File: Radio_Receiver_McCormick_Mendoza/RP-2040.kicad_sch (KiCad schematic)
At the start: 0 parts

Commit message: Merge conflict resolution.
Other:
- title: (none) -> Radio Receiver
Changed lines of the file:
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@@
 	(paper "A4")
 	(title_block
+		(title "Radio Receiver")
 		(date "2026-04-19")
 		(rev "0.0.1")

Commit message: Propogated Title Block Fields
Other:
- company: (none) -> Walla Walla University
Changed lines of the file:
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@@
 		(date "2026-04-19")
 		(rev "0.0.1")
+		(company "Walla Walla University")
 		(comment 2 "Daniel Mendoza")
 		(comment 3 "Jeffrey McCormick")

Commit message: Added switchable antenna filters and photos.
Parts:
- added J21: Conn_01x20_Socket, Connector_PinSocket_2.54mm:PinSocket_1x20_P2.54mm_Vertical, symbol Connector:Conn_01x20_Socket
- added J22: Conn_01x01_Pin, Connector_PinHeader_2.54mm:PinHeader_1x01_P2.54mm_Vertical, symbol Connector:Conn_01x01_Pin
- added J23: Conn_01x20_Socket, Intro_to_CAD:PinSocket_1x20_P2.54mm_Vertical-pins21-40, symbol Connector:Conn_01x20_Socket
- added JP50: USB Only, Jumper:SolderJumper-2_P1.3mm_Open_RoundedPad1.0x1.5mm, symbol Jumper:Jumper_2_Open
- added R29: 20kΩ, PCM_JLCPCB:R_0805, symbol PCM_JLCPCB-Resistors:0805,20kΩ
- added S1: Tactile Button, 160gf, PCM_JLCPCB:SW_TS-1088-AR02016, symbol PCM_JLCPCB-Connectors_Buttons:Tactile Button, 160gf, 12V, 50mA, 4.0mm
- added U13: Pico, MCU_RaspberryPi_and_Boards:RPi_Pico_SMD_TH, symbol MCU_RaspberryPi_and_Boards:Pico
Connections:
- new net: J21.1 (Pin_1), U13.1 (GPIO0)
- new net: J21.10 (Pin_10), U13.10 (GPIO7)
- new net: J21.11 (Pin_11), U13.11 (GPIO8)
- new net: J21.12 (Pin_12), U13.12 (GPIO9)
- new net: J21.14 (Pin_14), U13.14 (GPIO10)
- new net: J21.15 (Pin_15), U13.15 (GPIO11)
- new net: J21.16 (Pin_16), U13.16 (GPIO12)
- new net: J21.17 (Pin_17), U13.17 (GPIO13)
- new net: J21.19 (Pin_19), U13.19 (GPIO14)
- new net: J21.2 (Pin_2), U13.2 (GPIO1)
- new net: J21.20 (Pin_20), U13.20 (GPIO15)
- new net: J23.21 (Pin_20), U13.21 (GPIO16)
- new net: J23.22 (Pin_19), U13.22 (GPIO17)
- new net: J23.24 (Pin_17), U13.24 (GPIO18)
- new net: J23.25 (Pin_16), U13.25 (GPIO19)
- new net: J23.26 (Pin_15), U13.26 (GPIO20)
- new net: J23.27 (Pin_14), U13.27 (GPIO21)
- new net: J23.29 (Pin_12), U13.29 (GPIO22)
- new net: J23.31 (Pin_10), U13.31 (GPIO26_ADC0)
- new net: J23.32 (Pin_9), U13.32 (GPIO27_ADC1)
- new net: J23.33 (Pin_8), U13.33 (AGND)
- new net: J23.34 (Pin_7), U13.34 (GPIO28_ADC2)
- new net: J23.35 (Pin_6), U13.35 (ADC_VREF)
- new net: J23.36 (Pin_5), U13.36 (3V3)
- new net: J23.37 (Pin_4), U13.37 (3V3_EN)
- new net: J23.39 (Pin_2), U13.39 (VSYS)
- new net: J21.4 (Pin_4), U13.4 (GPIO2)
- new net: J22.1 (Pin_1), J23.40 (Pin_1), JP50.1 (A), U13.40 (VBUS)
- new net: J21.5 (Pin_5), U13.5 (GPIO3)
- new net: J21.6 (Pin_6), U13.6 (GPIO4)
- new net: J21.7 (Pin_7), U13.7 (GPIO5)
- new net: J21.9 (Pin_9), U13.9 (GPIO6)
- new net +3.3V: R29.1
- new net GND: J21.13 (Pin_13), J21.18 (Pin_18), J21.3 (Pin_3), J21.8 (Pin_8), J23.23 (Pin_18), J23.28 (Pin_13), J23.38 (Pin_3), S1.2 (B), U13.13 (GND), U13.18 (GND), U13.23 (GND), U13.28 (GND), U13.3 (GND), U13.38 (GND), U13.8 (GND)
- new net RST: J23.30 (Pin_11), R29.2, S1.1 (A), U13.30 (RUN)
- new net VDDA: JP50.2 (B)
- no-connect marks 0 -> 3
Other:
- note added: "If you are using a real Pico, his jumper bridges a Schottky diode from USB in to Vsys (4.7v with it open, 5.0v from USB port with it soldered)"
- note added: "These jumpers are for changing GPIO pins if necessary. They also allow you to connect modules similar to a breadboard."
- note added: "V+ (YD-RP2040) VBUS (Pico)"

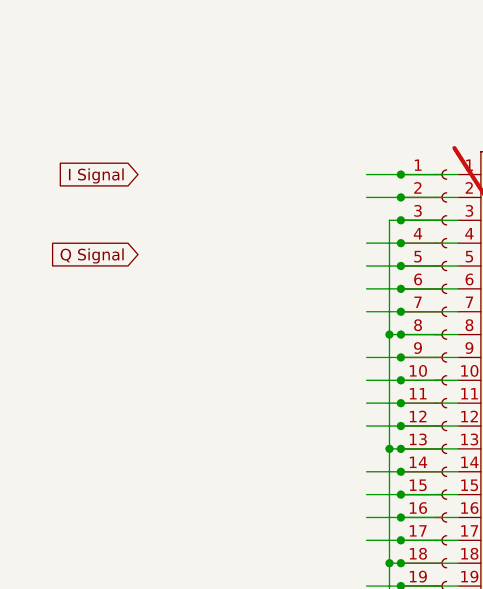
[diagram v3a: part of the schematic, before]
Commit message: Schematic connection edits
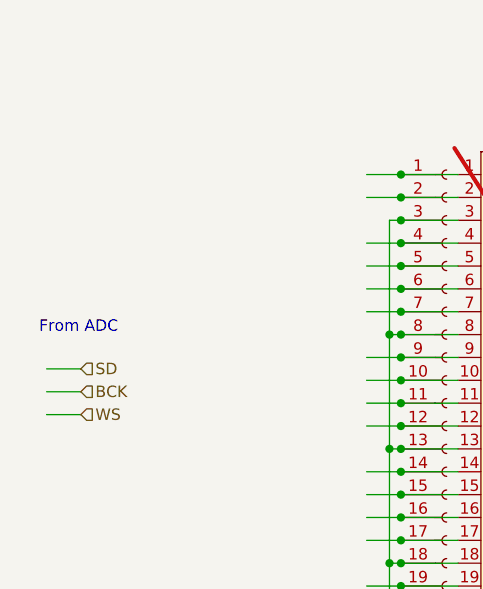
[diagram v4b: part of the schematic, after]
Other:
- note added: "From ADC"
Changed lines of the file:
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@@
+		)
+	)
+	(text "From ADC"
+		(exclude_from_sim no)
+		(at 63.246 83.058 0)
+		(effects
+			(font
+				(size 1.27 1.27)
+			)
 		)
 	)
@@
 	(wire
 		(pts
+			(xy 59.69 90.17) (xy 63.5 90.17)
+		)
+		(stroke
+			(width 0)
+			(type default)
+		)
+	)
+	(wire
+		(pts
 			(xy 97.79 71.12) (xy 99.06 71.12)
 		)
@@
 	(wire
 		(pts
+			(xy 59.69 87.63) (xy 63.5 87.63)
+		)
+		(stroke
+			(width 0)
+			(type default)
+		)
+	)
+	(wire
+		(pts
 			(xy 149.86 71.12) (xy 153.67 71.12)
 		)
@@
 		(pts
 			(xy 140.97 88.9) (xy 147.32 88.9)
+		)
+		(stroke
+			(width 0)
+			(type default)
+		)
+	)
+	(wire
+		(pts
+			(xy 59.69 92.71) (xy 63.5 92.71)
 		)
 		(stroke
@@
 		)
 	)
-	(global_label "Q Signal"
+	(hierarchical_label "SD"
 		(shape input)
-		(at 69.85 74.93 180)
-		(fields_autoplaced yes)
+		(at 63.5 87.63 0)
 		(effects
 			(font
 				(size 1.27 1.27)
 			)
-			(justify right)
-		)
-		(property "Intersheetrefs" "${INTERSHEET_REFS}"
-			(at 58.6402 74.93 0)
-			(hide yes)
-			(show_name no)
-			(do_not_autoplace no)
-			(effects
-				(font
-					(size 1.27 1.27)
-				)
-				(justify right)
-			)
-		)
-	)
-	(global_label "I Signal"
+			(justify left)
+		)
+	)
+	(hierarchical_label "BCK"
 		(shape input)
-		(at 69.85 66.04 180)
-		(fields_autoplaced yes)
+		(at 63.5 90.17 0)
 		(effects
 			(font
 				(size 1.27 1.27)
 			)
-			(justify right)
-		)
-		(property "Intersheetrefs" "${INTERSHEET_REFS}"
-			(at 59.3659 66.04 0)
-			(hide yes)
-			(show_name no)
-			(do_not_autoplace no)
-			(effects
-				(font
-					(size 1.27 1.27)
-				)
-				(justify right)
+			(justify left)
+		)
+	)
+	(hierarchical_label "WS"
+		(shape input)
+		(at 63.5 92.71 0)
+		(effects
+			(font
+				(size 1.27 1.27)
 			)
-		)
-	)
+			(justify left)
+		)
+	)
